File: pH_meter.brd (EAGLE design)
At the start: 45.1 x 15 mm, 45 parts, among them IC1 W25Q64JVXGIQ, J3 TF-123-ARP9HXX, U1 RP2040, U3 MIC5504-3.3YM5_TR

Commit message: Daily check-in
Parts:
- removed CONN1: GT-USB_8012A, GT_USB-8012A:GT-USB-8012A
- added C18, C22, C23, C24, C29, C31, C32, C33: 0.1uF, SparkFun-Capacitors:0603
- added C25, C26, C28, C30: 10uF, SparkFun-Capacitors:0603
- added C27: 0.1uF, SparkFun-Capacitors:0402
- added J1: TYPE-C-31-M-12, TYPE-C-31-M-12:HRO_TYPE-C-31-M-12
- added J4, J5: 60312202114511, 60312202114511:60312202114511
- added R11: 10k, SparkFun-Resistors:0603
- added R12, R13: 2.2k, SparkFun-Resistors:0603
- added R15, R16, R17, R18: (no value), SparkFun-Resistors:0402
- added R9: 16.9k, SparkFun-Resistors:0603
- added U$1, U$2: PH-OEM, pH-OEM:PH_SENSOR
- added U2: BME280, BME280:PSON65P250X250X100-8N
- added U4: ADM3260ARSZ, ADM3260ARSZ:SSOP20
- added U5: SFH6325-X017T, SFH6325-X017T:SOIC254P1030X460-8N
- C12, C13, C19: device SparkFun-Capacitors:0402 -> SparkFun-Capacitors:0603
- C14, C15: device OPL_Capacitor:C0402 -> SparkFun-Capacitors:0603
- L1: value 2.2nH -> LQW18AN2N2D10D; device SparkFun-Coils:0402 -> LQW18AN2N2D10D:INDC1608X100N
- R1, R2: value 27 -> (none)
- R10: value 330 -> (none)
- R14: value 1K -> (none)
- R3, R8: value 5.1K -> 5.1k; device SparkFun-Resistors:0402 -> SparkFun-Resistors:0603
- R4: value DNF -> (none)
- R5: value 10K -> (none)
- R6, R7: value 2.2K -> 2.2k; device SparkFun-Resistors:0402 -> SparkFun-Resistors:0603
- moved L1 112.2 mm to (-30.7, -101.3), flipped to the top, turned to 0 degrees
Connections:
- new net GND-ISO: C24.2, C26.2, C30.2, C31.2, C32.2, C33.2, R11.1, U$1.P$6, U$2.P$6, U4.P11, U4.P14, U4.P16, U4.P20, U5.2, U5.3
- new net INT_MOD1: R15.1, U1.2, U5.7
- new net INT_MOD1ISO: R18.1, U$2.P$7
- new net INT_MOD2: R16.1, U1.3, U5.6
- new net INT_MOD2ISO: R17.1, U$1.P$7
- new net N$2: R11.2, R9.1, U4.P13
- new net N$5: J1.B5, R8.2
- new net N$8: R18.2, U5.1
- new net PDIS: U1.31, U4.P8
- new net PROBE: J4.1, U$2.P$4
- new net PROBE2: J5.1, U$1.P$4
- new net PROBE2_GND: J5.2, J5.3, U$1.P$5
- new net PROBE_GND: J4.2, J4.3, U$2.P$5
- new net SCL_ISO: R13.1, U$1.P$8, U$2.P$8, U4.P19
- new net SDA_ISO: R12.1, U$1.P$1, U$2.P$1, U4.P18
- new net VCC-ISO: C24.1, C26.1, C30.1, C31.1, C32.1, C33.1, R12.2, R13.2, R9.2, U$1.P$3, U$2.P$3, U4.P12, U4.P17
- net 3.3V: now also C18.1, C22.1, C27.2, C28.1, C29.1, R15.2, R16.2, U2.2, U2.6, U2.8, U4.P4, U5.8
- net GND: now also C18.2, C22.2, C23.2, C25.2, C27.1, C28.2, C29.2, J1.A1_B12, J1.B1_A12, J1.S1, J1.S2, J1.S3, J1.S4, U2.1, U2.5, U2.7, U4.P1, U4.P10, U4.P5, U4.P7, U5.5; no longer CONN1.A1, CONN1.A12, CONN1.B1, CONN1.B12, CONN1.TH1, CONN1.TH2
- net N$3: now also J1.A5; no longer CONN1.A5
- net N$7: now also R17.2, U5.4; no longer CONN1.B5, R8.2
- net N$9: now also J1.A4_B9, J1.B4_A9; no longer CONN1.A4, CONN1.A9, CONN1.B4, CONN1.B9
- net SCL: now also U2.4, U4.P2
- net SDA: now also U2.3, U4.P3
- net USB_N: now also J1.A7, J1.B7; no longer CONN1.A7, CONN1.B7
- net USB_P: now also J1.A6, J1.B6; no longer CONN1.A6, CONN1.B6
- net V_USB: now also C23.1, C25.1, U4.P9
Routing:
- net N$7: track 7.68 -> 0.00 mm, vias 1 -> 0
- net USB_P: track 9.45 -> 5.23 mm, vias 2 -> 0
- net N$3: track 3.60 -> 0.00 mm, vias 1 -> 0
- net N$9: track 32.6 -> 30.1 mm
- net USB_N: track 7.19 -> 4.77 mm
- net 3.3V: track 94.2 -> 93.0 mm
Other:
- board size 45.1 x 15 mm -> 69.3 x 109.1 mm

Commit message: Partial component placement
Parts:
- removed D2: BLUE-0402, OPL_Optoelectronics:LED-0402
- added D1: (no value), SparkFun-LED:LED-0603
- C1, C10, C11, C16, C17, C2, C27, C3, C4, C5, C6, C7, C8, C9: device SparkFun-Capacitors:0402 -> SparkFun-Capacitors:0603
- C20, C21: value 33pf -> 33pF; device OPL_Capacitor:C0402 -> SparkFun-Capacitors:0603
- R1, R2: value (none) -> 27; device SparkFun-Resistors:0402 -> SparkFun-Resistors:0603
- R10, R17, R18: value (none) -> 100; device SparkFun-Resistors:0402 -> SparkFun-Resistors:0603
- R14, R15, R16, R5: value (none) -> 1k; device SparkFun-Resistors:0402 -> SparkFun-Resistors:0603
- R4: device SparkFun-Resistors:0402 -> SparkFun-Resistors:0603
- R9: value 16.9k -> 16.2k
- moved L1 170.7 mm to (42.4, 52.9)
- moved C23 155.3 mm to (41.5, 32.7)
- moved J4 155.0 mm to (52.6, 3.94)
- moved C25 124.0 mm to (27.7, 1.27)
- moved U5 115.1 mm to (16.8, 30.5), turned to 90 degrees
- moved C24 105.9 mm to (47.2, 19.9)
- moved J5 102.3 mm to (-61.7, -119.1)
- moved U4 97.9 mm to (42.7, 26.2), turned to 180 degrees
- moved J1 92.0 mm to (30.7, 57.4), turned to 180 degrees
- moved C26 88.2 mm to (33.5, 2.03), turned to 270 degrees
- moved R9 87.9 mm to (27.6, 2.69), turned to 180 degrees
- moved C22 75.0 mm to (27.1, 13.8), turned to 180 degrees
- moved C14 66.9 mm to (46.7, 51.2), flipped to the top, turned to 270 degrees
- moved C13 64.9 mm to (45.1, 51.2), flipped to the top
- moved C12 62.2 mm to (39.7, 53.7), flipped to the top, turned to 90 degrees
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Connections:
- removed net INT_ZMOD4510: U1.34
- removed net RES_ZMOD4510: U1.32
- net GND: now also D1.C; no longer D2.-
- net N$1: now also D1.A; no longer D2.+
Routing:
- net 3.3V: track 93.0 -> 0.00 mm, vias 14 -> 0
- net SCL: track 42.6 -> 0.00 mm, vias 3 -> 0
- net VOUT: track 35.8 -> 0.00 mm, vias 3 -> 0
- net N$9: track 30.1 -> 0.00 mm, vias 2 -> 0
- net SDO: track 29.3 -> 0.00 mm, vias 2 -> 0
- net SDA: track 28.6 -> 0.00 mm, vias 3 -> 0
- net INT_ZMOD4510: track 28.4 -> 0.00 mm, vias 2 -> 0
- net SWITCH: track 28.4 -> 0.00 mm, vias 2 -> 0
- net QSPI_CS: track 23.4 -> 0.00 mm, vias 2 -> 0
- net DATA1: track 22.3 -> 0.00 mm, vias 2 -> 0
- net RES_ZMOD4510: track 22.1 -> 0.00 mm, vias 2 -> 0
- net SDI: track 21.9 -> 0.00 mm, vias 2 -> 0
- net QSPI_SD2: track 20.3 -> 0.00 mm, vias 2 -> 0
- net SWD: track 20.2 -> 0.00 mm, vias 1 -> 0
- net NEOPIXEL: track 18.6 -> 0.00 mm, vias 2 -> 0
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- removed copper zone on layer 15, net 3.3V
- removed copper zone on layer 1, net GND
- removed copper zone on layer 16, net GND
- removed copper zone on layer 2, net GND
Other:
- board size 69.3 x 109.1 mm -> 59.1 x 59.1 mm
- board text removed: "Air Fobulous 2040"
- board text removed: "GND"
- board text removed: "SWD"

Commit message: Generated gerbers
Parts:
- added C34: 0.1uF, SparkFun-Capacitors:0603
- moved C29 170.8 mm to (46.9, 37.5), turned to 180 degrees
- moved C28 166.5 mm to (46.9, 35.9), turned to 180 degrees
- moved C31 164.4 mm to (40.4, 26.9), turned to 270 degrees
- moved C30 162.3 mm to (48.5, 23.6)
- moved J5 158.4 mm to (38.1, 3.81)
- moved C33 155.9 mm to (41.1, 7.65), turned to 180 degrees
- moved C32 140.0 mm to (15.2, 7.65), turned to 180 degrees
- moved C27 130.7 mm to (8.89, 33.0)
- moved R13 130.4 mm to (54.4, 25.5)
- moved R12 129.0 mm to (54.4, 27.1)
- moved R18 128.2 mm to (13.0, 22.4), turned to 90 degrees
- moved R17 127.9 mm to (20.6, 22.4), turned to 90 degrees
- moved R16 123.2 mm to (8.92, 28.5), turned to 180 degrees
- moved R15 121.5 mm to (8.92, 30.0), turned to 180 degrees
- moved C18 116.6 mm to (49.4, 52.3), turned to 180 degrees
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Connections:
- net 3.3V: now also C34.1
- net GND: now also C34.2
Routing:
- net 3.3V: track 0.00 -> 113.1 mm, vias 0 -> 19
- net SDA_ISO: track 0.00 -> 69.8 mm, vias 0 -> 4
- net SCL: track 0.00 -> 59.7 mm
- net SDA: track 0.00 -> 58.9 mm
- net SCL_ISO: track 0.00 -> 57.4 mm, vias 0 -> 2
- net SWCLK: track 0.00 -> 51.6 mm, vias 0 -> 2
- net INT_MOD2ISO: track 0.00 -> 51.3 mm
- net SDI: track 0.00 -> 44.0 mm
- net SWD: track 0.00 -> 43.9 mm, vias 0 -> 2
- net V_USB: track 0.00 -> 43.3 mm, vias 0 -> 2
- net VOUT: track 0.00 -> 41.5 mm, vias 0 -> 3
- net DATA2: track 0.00 -> 40.6 mm, vias 0 -> 2
- net CLK: track 0.00 -> 40.5 mm
- net CS: track 0.00 -> 40.0 mm, vias 0 -> 2
- net SWITCH: track 0.00 -> 40.0 mm, vias 0 -> 2
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- added copper zone on layer 15, net 3.3V
- added copper zone on layer 1, net GND
- added copper zone on layer 16, net GND
- added copper zone on layer 2, net GND
- added copper zone on layer 1, net GND-ISO
- added copper zone on layer 16, net GND-ISO
- added copper zone on layer 2, net GND-ISO
- added copper zone on layer 1, net PROBE2_GND
- added copper zone on layer 16, net PROBE2_GND
- added copper zone on layer 2, net PROBE2_GND
- added copper zone on layer 1, net PROBE_GND
- added copper zone on layer 16, net PROBE_GND
- added copper zone on layer 2, net PROBE_GND
- added copper zone on layer 15, net VCC-ISO
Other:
- board text added: "GND"
- board text added: "SWD"

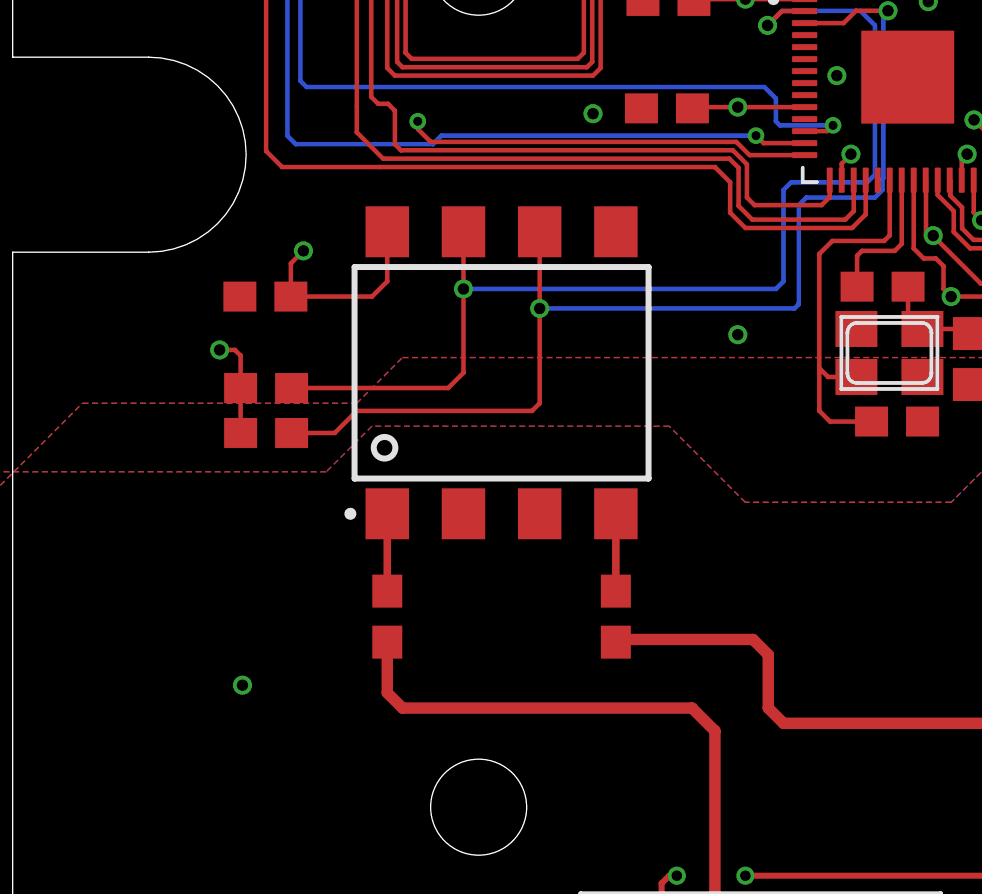
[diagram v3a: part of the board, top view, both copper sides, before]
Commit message: Changes to accommodate BoM costs
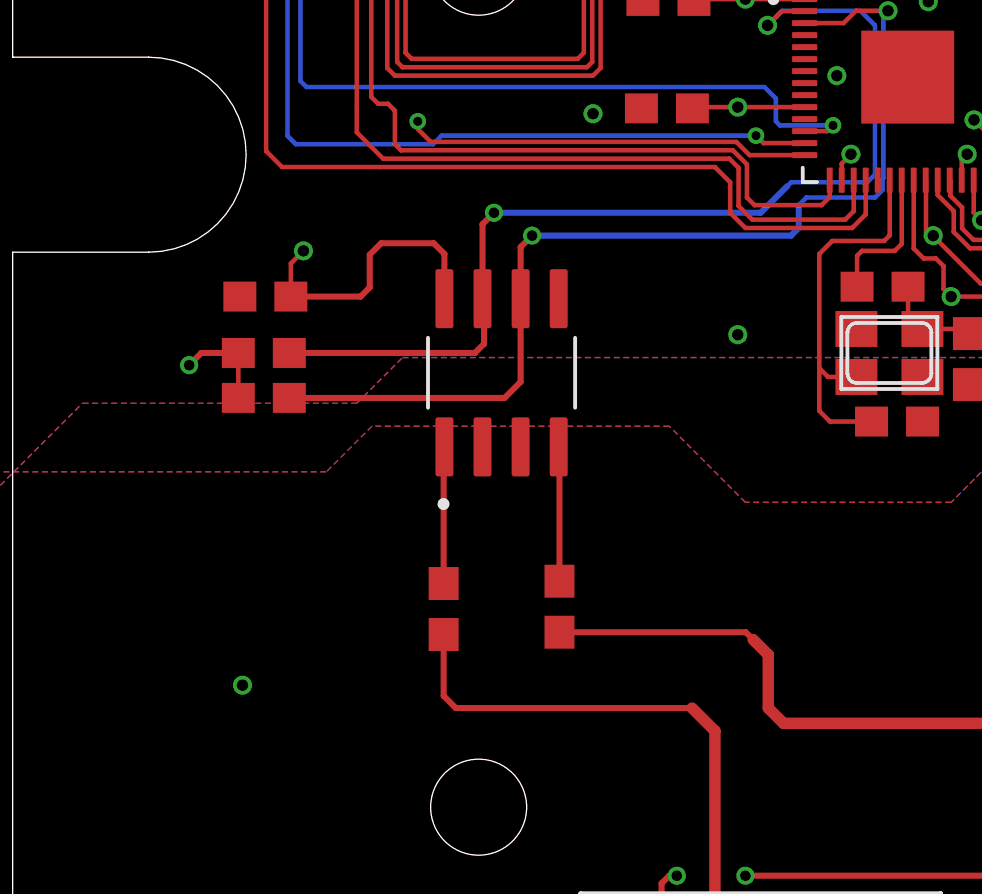
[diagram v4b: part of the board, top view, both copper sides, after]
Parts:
- U5: value SFH6325-X017T -> SFH6325-X017TEL0631; device SFH6325-X017T:SOIC254P1030X460-8N -> SFH6325-X017T:SOIC127P599X175-8N
- moved R17 1.91 mm to (18.7, 22.7)
- moved R18 1.90 mm to (14.8, 22.6)
- moved R15 1.17 mm to (8.84, 31.1)
- moved R16 1.17 mm to (8.84, 29.6)
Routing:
- net INT_MOD2: track 38.4 -> 34.7 mm
- net INT_MOD1: track 38.1 -> 35.0 mm
- net INT_MOD2ISO: track 51.3 -> 53.4 mm
- net 3.3V: track 113.1 -> 115.2 mm
- net N$8: track 2.58 -> 4.56 mm
- net N$7: track 2.58 -> 4.49 mm
- net INT_MOD1ISO: track 33.6 -> 32.0 mm
